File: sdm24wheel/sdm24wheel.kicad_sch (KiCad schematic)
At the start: 47 parts, among them J1 ATM15-08PA, J2 SWD, J3 USB_B_Micro, SW1 BOOT, U1 STM32F072CBT6, U2 MLX90614, U3 MIC37100-3.3WS, U4 24LC01BT-E/LT, U5 SN65HVD230, U6 USBLC6-2SC6, Y1 8MHz

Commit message: owo
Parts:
- C12: footprint Capacitor_SMD:C_0603_1608Metric -> Capacitor_SMD:C_0402_1005Metric
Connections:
- net CAN+: now also J1.1 (Pin_1); no longer J1.8 (Pin_8)
- net CAN-: now also J1.8 (Pin_8); no longer J1.1 (Pin_1)
- net GND: now also J1.2 (Pin_2), J1.3 (Pin_3); no longer J1.5 (Pin_5), J1.7 (Pin_7)
- net HE_OUTPUT: now also J1.5 (Pin_5), U1.40 (PB4); no longer J1.4 (Pin_4), U1.20 (PB2)
- net USR_LED: now also U1.13 (PA3); no longer U1.25 (PB12)
- net VCC: now also J1.6 (Pin_6), J1.7 (Pin_7); no longer J1.2 (Pin_2), J1.3 (Pin_3)
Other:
- moved on the sheet: D4, R6

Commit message: updating repo
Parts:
- removed C10, C13, C7, C8, C9: 100nF, Capacitor_SMD:C_0402_1005Metric, symbol Device:C_Small
- removed C11, C6: 4.7uF, Capacitor_SMD:C_0805_2012Metric, symbol Device:C_Small
- removed C12: 10nF, Capacitor_SMD:C_0402_1005Metric, symbol Device:C_Small
- removed C14, C15: 1uF, Capacitor_SMD:C_0805_2012Metric, symbol Device:C_Small
- removed D4: GREEN, Library:Dialight_561-XX0X-XXX, symbol Device:LED_Small
- removed FB1: 120R, Inductor_SMD:L_0603_1608Metric, symbol Device:FerriteBead_Small
- removed R4, R5: 4.7k, Resistor_SMD:R_0805_2012Metric, symbol Device:R_Small
- removed R6: 220, Resistor_SMD:R_0805_2012Metric, symbol Device:R_Small
- removed R7: 10k, Resistor_SMD:R_0805_2012Metric, symbol Device:R_Small
- removed SW1: BOOT, Library:Gravitech_MINI-SPDT-SW, symbol Switch:SW_SPDT
- removed U1: STM32F072CBT6, Package_QFP:LQFP-48_7x7mm_P0.5mm, symbol MCU_ST_STM32F0:STM32F072C8Tx
- removed Y1: 8MHz, Crystal:Crystal_SMD_Abracon_ABM3C-4Pin_5.0x3.2mm, symbol Device:Crystal_GND24
- added U1: STM32F405RGTx, Package_QFP:LQFP-64_10x10mm_P0.5mm, symbol MCU_ST_STM32F4:STM32F405RGTx
- C3, C5: value 10pF -> 2.2uF; footprint Capacitor_SMD:C_0603_1608Metric -> (none)
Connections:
- net +3.3V: now also U1.1 (VBAT), U1.19 (VDD), U1.32 (VDD), U1.48 (VDD), U1.64 (VDD)
- net +3.3VA: now also U1.13 (VDDA)
- net GND: now also U1.12 (VSSA), U1.18 (VSS), U1.63 (VSS)
- net HSE_IN: now also U1.5 (PH0); no longer C3.1
- net HSE_OUT: now also U1.6 (PH1); no longer C5.1
- net SWCLK: now also U1.49 (PA14)
- net SWDIO: now also U1.46 (PA13)
- new net: C5.1, U1.31 (VCAP_1)
- new net: C3.1, U1.47 (VCAP_2)
- new net NRST: U1.7 (NRST)
- new net SWO: U1.55 (PB3)
- no-connect marks 29 -> 4
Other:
- note added: "ESR < 2"
- note removed: "EA3250QA10-8.000M Load Capacitance: 10pF"
- note removed: "STM32F072x8"
- note removed: "disable internal pull-up/down resistors per 6.2 in datasheet"

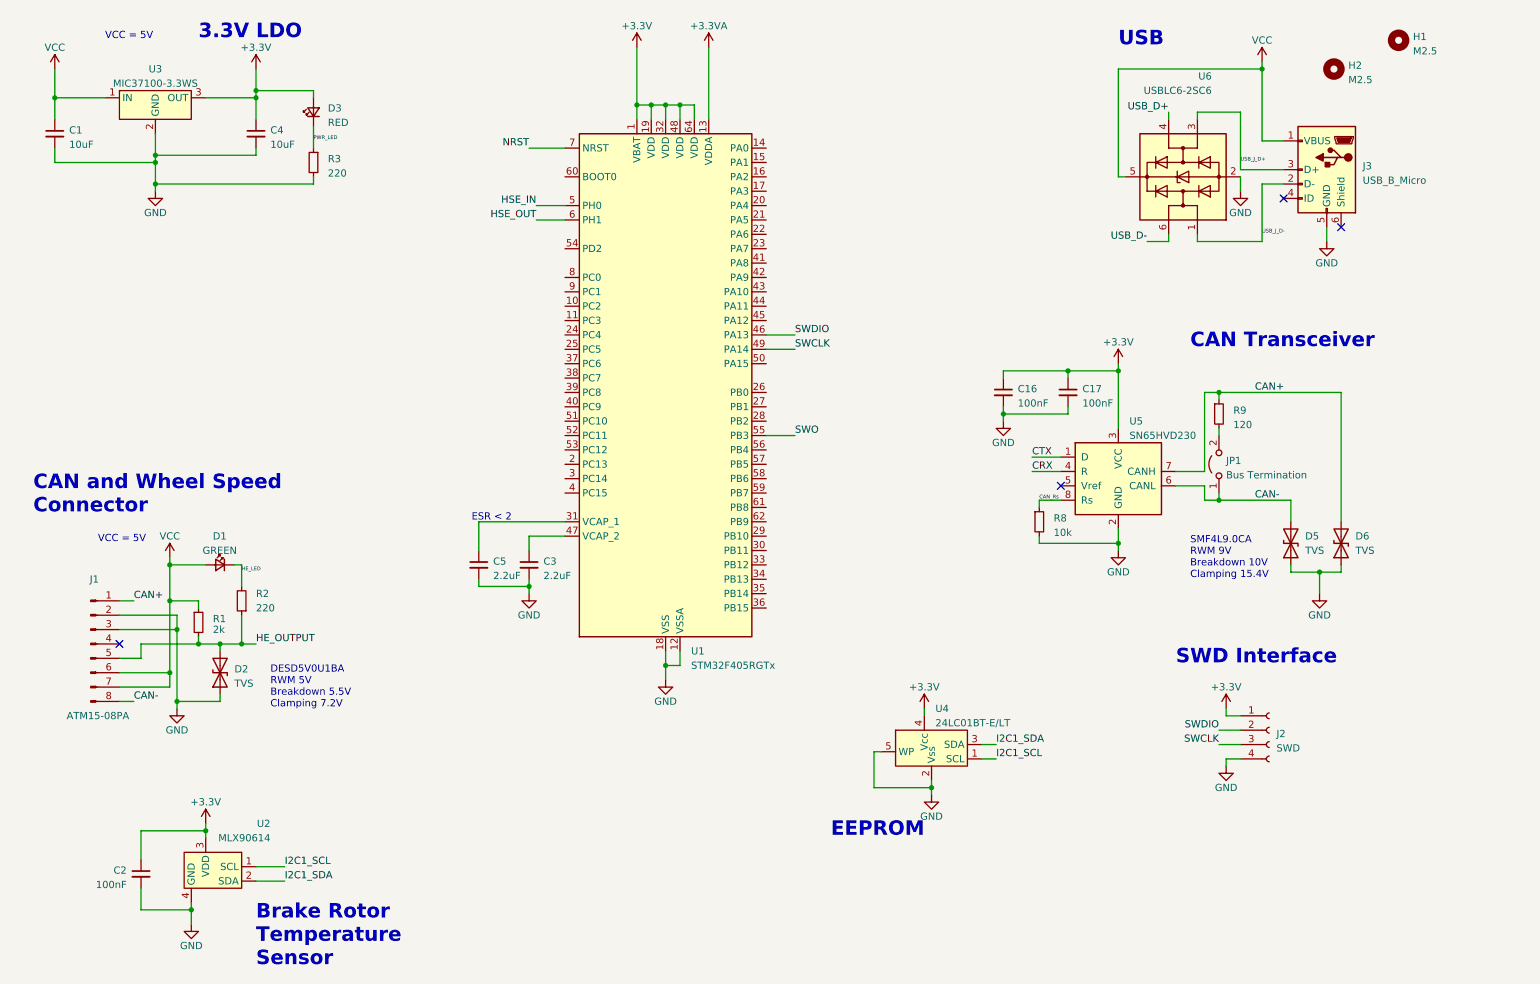
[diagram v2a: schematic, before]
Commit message: wheel board updates
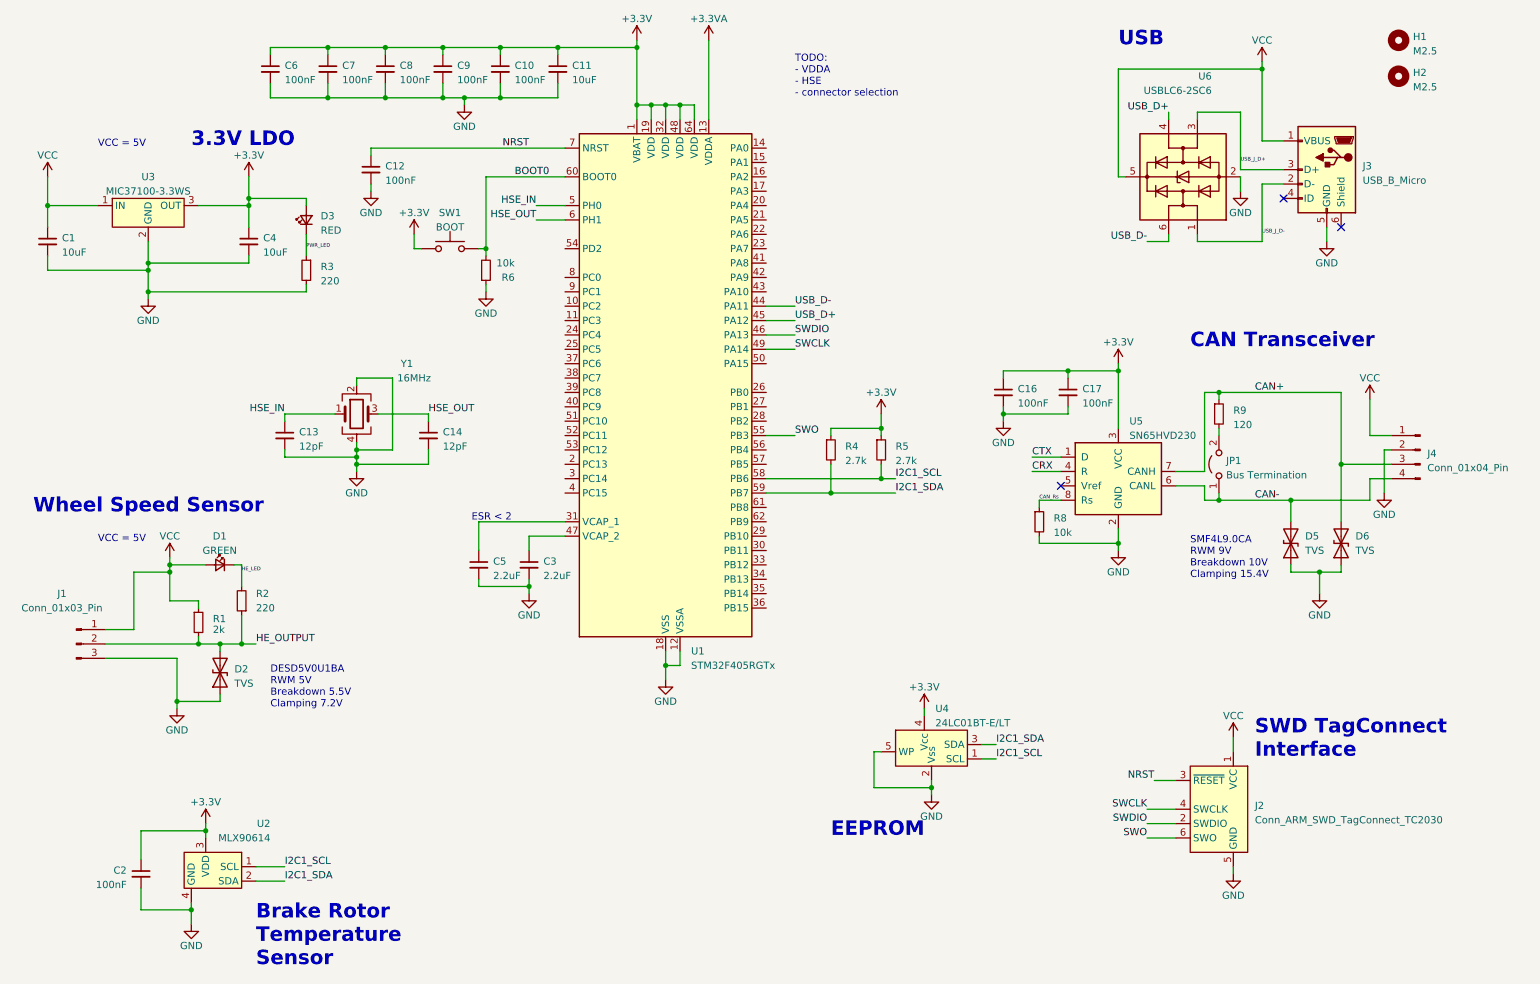
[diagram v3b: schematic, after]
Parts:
- removed J1: ATM15-08PA, Library:ATM15-08PX-BMXX, symbol Connector:Conn_01x08_Pin
- removed J2: SWD, Connector_PinSocket_2.54mm:PinSocket_1x04_P2.54mm_Vertical, symbol Connector:Conn_01x04_Socket
- added C10, C12, C6, C7, C8, C9: 100nF, symbol Device:C_Small
- added C11: 10uF, symbol Device:C_Small
- added C13, C14: 12pF, symbol Device:C_Small
- added J1: Conn_01x03_Pin, symbol Connector:Conn_01x03_Pin
- added J2: Conn_ARM_SWD_TagConnect_TC2030, Connector:Tag-Connect_TC2030-IDC-FP_2x03_P1.27mm_Vertical, symbol Connector:Conn_ARM_SWD_TagConnect_TC2030
- added J4: Conn_01x04_Pin, symbol Connector:Conn_01x04_Pin
- added R4, R5: 2.7k, Resistor_SMD:R_0805_2012Metric, symbol Device:R_Small
- added R6: 10k, Resistor_SMD:R_0805_2012Metric, symbol Device:R_Small
- added SW1: BOOT, symbol Switch:SW_Push
- added Y1: 16MHz, symbol Device:Crystal_GND24
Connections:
- net +3.3V: now also C10.1, C11.1, C6.1, C7.1, C8.1, C9.1, R4.1, R5.1, SW1.1
- net CAN+: now also J4.3 (Pin_3)
- net CAN-: now also J4.4 (Pin_4)
- net GND: now also C10.2, C11.2, C12.2, C13.2, C14.2, C6.2, C7.2, C8.2, C9.2, J1.3 (Pin_3), J2.5 (GND), J4.2 (Pin_2), R6.1, Y1.2, Y1.4
- net HE_OUTPUT: now also J1.2 (Pin_2)
- net HSE_IN: now also C13.1, Y1.1
- net HSE_OUT: now also C14.1, Y1.3
- net I2C1_SCL: now also U1.58 (PB6), R5.2
- net I2C1_SDA: now also U1.59 (PB7), R4.2
- net NRST: now also C12.1, J2.3 (~{RESET})
- net SWCLK: now also J2.4 (SWCLK)
- net SWDIO: now also J2.2 (SWDIO)
- net SWO: now also J2.6 (SWO)
- net USB_D+: now also U1.45 (PA12)
- net USB_D-: now also U1.44 (PA11)
- net VCC: now also J1.1 (Pin_1), J2.1 (VCC), J4.1 (Pin_1)
- net BOOT0: now reaches U1.60 (BOOT0)
- net BOOT0: now also R6.2, SW1.2
- no-connect marks 4 -> 3
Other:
- note added: "SWD TagConnect Interface"
- note added: "TODO: - VDDA - HSE - connector selection"
- note added: "Wheel Speed Sensor"
- note removed: "CAN and Wheel Speed Connector"
- note removed: "SWD Interface"
- moved on the sheet: C1, C4, D3, H2, R3, U3

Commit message: wheel board rework
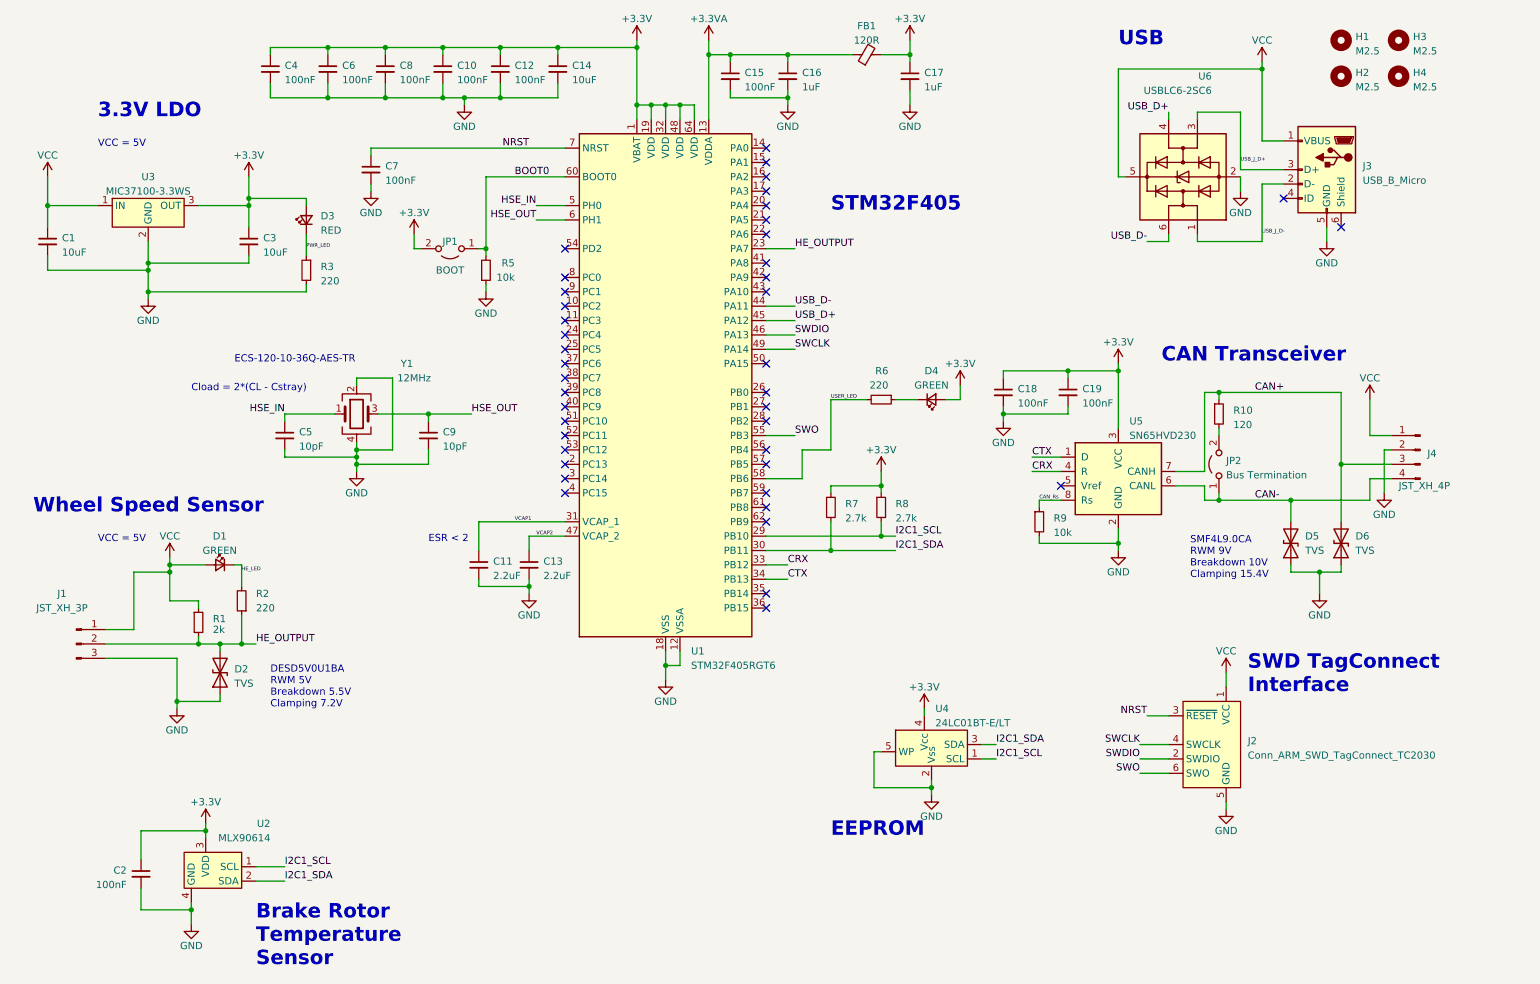
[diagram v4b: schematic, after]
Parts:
- removed R4, R5: 2.7k, Resistor_SMD:R_0805_2012Metric, symbol Device:R_Small
- removed SW1: BOOT, symbol Switch:SW_Push
- added C15: 100nF, Capacitor_SMD:C_0402_1005Metric, symbol Device:C_Small
- added C16, C17: 1uF, Capacitor_SMD:C_0603_1608Metric, symbol Device:C_Small
- added D4: GREEN, Library:Dialight_561-XX0X-XXX, symbol Device:LED_Small
- added FB1: 120R, Inductor_SMD:L_0603_1608Metric, symbol Device:FerriteBead_Small
- added H3, H4: M2.5, MountingHole:MountingHole_2.7mm_M2.5, symbol Mechanical:MountingHole
- added JP1: BOOT, Connector_PinHeader_2.54mm:PinHeader_1x02_P2.54mm_Vertical, symbol Jumper:Jumper_2_Open
- added R6: 220, Resistor_SMD:R_0805_2012Metric, symbol Device:R_Small
- added R7, R8: 2.7k, Resistor_SMD:R_0603_1608Metric, symbol Device:R_Small
- C10: renamed from C9; footprint (none) -> Capacitor_SMD:C_0402_1005Metric
- C11: renamed from C5; footprint (none) -> Capacitor_SMD:C_0603_1608Metric
- C12: renamed from C10; footprint (none) -> Capacitor_SMD:C_0402_1005Metric
- C13: renamed from C3; footprint (none) -> Capacitor_SMD:C_0603_1608Metric
- C14: renamed from C11; footprint (none) -> Capacitor_SMD:C_0805_2012Metric
- C4: renamed from C6; footprint (none) -> Capacitor_SMD:C_0402_1005Metric
- C5: renamed from C13; value 12pF -> 10pF; footprint (none) -> Capacitor_SMD:C_0402_1005Metric
- C6: renamed from C7; footprint (none) -> Capacitor_SMD:C_0402_1005Metric
- C7: renamed from C12; footprint (none) -> Capacitor_SMD:C_0402_1005Metric
- C8: footprint (none) -> Capacitor_SMD:C_0402_1005Metric
- C9: renamed from C14; value 12pF -> 10pF; footprint (none) -> Capacitor_SMD:C_0402_1005Metric
- J1: value Conn_01x03_Pin -> JST_XH_3P; footprint (none) -> Connector_JST:JST_XH_B3B-XH-AM_1x03_P2.50mm_Vertical
- J2: footprint Connector:Tag-Connect_TC2030-IDC-FP_2x03_P1.27mm_Vertical -> Connector:Tag-Connect_TC2030-IDC-NL_2x03_P1.27mm_Vertical
- J4: value Conn_01x04_Pin -> JST_XH_4P; footprint (none) -> Connector_JST:JST_XH_B4B-XH-AM_1x04_P2.50mm_Vertical
- U1: value STM32F405RGTx -> STM32F405RGT6
- Y1: value 16MHz -> 12MHz; footprint (none) -> Crystal:Crystal_SMD_2520-4Pin_2.5x2.0mm
- renumbered C16 to C18, C17 to C19, C4 to C3, JP1 to JP2, R9 to R10, R6 to R5, R8 to R9
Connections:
- net +3.3V: now also C17.1, D4.2 (A), FB1.2, JP1.2 (B), R7.1, R8.1
- net +3.3VA: now also C15.1, C16.1, FB1.1
- net BOOT0: now also JP1.1 (A)
- net CRX: now also U1.33 (PB12)
- net CTX: now also U1.34 (PB13)
- net GND: now also C15.2, C16.2, C17.2
- net HE_OUTPUT: now also U1.23 (PA7)
- net I2C1_SCL: now also U1.29 (PB10), R8.2; no longer U1.58 (PB6)
- net I2C1_SDA: now also U1.30 (PB11), R7.2; no longer U1.59 (PB7)
- net VCAP1: now reaches C11.1, U1.31 (VCAP_1)
- net VCAP2: now reaches C13.1, U1.47 (VCAP_2)
- new net: D4.1 (K), R6.1
- new net USER_LED: R6.2, U1.58 (PB6)
- no-connect marks 3 -> 41
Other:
- note added: "Cload = 2*(CL - Cstray)"
- note added: "ECS-120-10-36Q-AES-TR"
- note added: "STM32F405"
- note removed: "TODO: - VDDA - HSE - connector selection"
- moved on the sheet: H1, H2, J2

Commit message: adding updates
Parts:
- removed H1, H3: M2.5, MountingHole:MountingHole_2.7mm_M2.5, symbol Mechanical:MountingHole
- renumbered H2 to H1, H4 to H2
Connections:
- net HE_OUTPUT: now also U1.16 (PA2); no longer U1.23 (PA7)
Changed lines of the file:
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@@
   (title_block
     (title "SDM-24 Wheel Board")
-    (date "2023-09-03")
+    (date "2023-09-04")
     (rev "v1")
     (company "Sun Devil Motorsports")
@@
   (no_connect (at 144.78 46.99))
   (no_connect (at 144.78 118.11))
-  (no_connect (at 144.78 41.91))
   (no_connect (at 144.78 82.55))
   (no_connect (at 109.22 69.85))
   (no_connect (at 109.22 85.09))
   (no_connect (at 144.78 92.71))
+  (no_connect (at 144.78 54.61))
   (no_connect (at 109.22 77.47))
   (no_connect (at 144.78 52.07))
@@
     (stroke (width 0) (type default))
   )
+  (wire (pts (xy 144.78 41.91) (xy 149.86 41.91))
+    (stroke (width 0) (type default))
+  )
   (wire (pts (xy 222.25 99.06) (xy 222.25 96.52))
     (stroke (width 0) (type default))
@@
   )
   (wire (pts (xy 85.09 92.71) (xy 72.39 92.71))
-    (stroke (width 0) (type default))
-  )
-  (wire (pts (xy 144.78 54.61) (xy 149.86 54.61))
     (stroke (width 0) (type default))
   )
@@
     (effects (font (size 1.27 1.27)) (justify left bottom))
   )
-  (text "STM32F405" (at 156.21 48.26 0)
+  (text "STM32F405" (at 163.83 48.26 0)
     (effects (font (size 2.56 2.56) (thickness 0.512) bold) (justify left bottom))
   )
@@
     (effects (font (size 0.65 0.65)) (justify left bottom))
   )
-  (label "HE_OUTPUT" (at 149.86 54.61 0) (fields_autoplaced)
+  (label "HE_OUTPUT" (at 149.86 41.91 0) (fields_autoplaced)
     (effects (font (size 1.27 1.27)) (justify left bottom))
   )
@@
     )
   )
-  (symbol (lib_id "Mechanical:MountingHole") (at 256.54 17.78 0) (unit 1)
-    (in_bom yes) (on_board yes) (dnp no) (fields_autoplaced)
-    (property "Reference" "H3" (at 259.08 17.145 0)
-      (effects (font (size 1.27 1.27)) (justify left))
-    )
-    (property "Value" "M2.5" (at 259.08 19.685 0)
-      (effects (font (size 1.27 1.27)) (justify left))
-    )
-    (property "Footprint" "MountingHole:MountingHole_2.7mm_M2.5" (at 256.54 17.78 0)
-      (effects (font (size 1.27 1.27)) hide)
-    )
-    (property "Datasheet" "~" (at 256.54 17.78 0)
-      (effects (font (size 1.27 1.27)) hide)
-    )
-    (instances
-      (project "sdm24wheel"
-        (path "/58bd889d-28e2-49da-85df-8e04b7f08117"
-          (reference "H3") (unit 1)
-        )
-      )
-    )
-  )
   (symbol (lib_id "power:VCC") (at 17.78 41.91 0) (unit 1)
     (in_bom yes) (on_board yes) (dnp no) (fields_autoplaced)
@@
   (symbol (lib_id "Mechanical:MountingHole") (at 246.38 24.13 0) (unit 1)
     (in_bom yes) (on_board yes) (dnp no) (fields_autoplaced)
-    (property "Reference" "H2" (at 248.92 23.495 0)
+    (property "Reference" "H1" (at 248.92 23.495 0)
       (effects (font (size 1.27 1.27)) (justify left))
     )
@@
       (project "sdm24wheel"
         (path "/58bd889d-28e2-49da-85df-8e04b7f08117"
-          (reference "H2") (unit 1)
+          (reference "H1") (unit 1)
         )
       )
@@
   (symbol (lib_id "Mechanical:MountingHole") (at 256.54 24.13 0) (unit 1)
     (in_bom yes) (on_board yes) (dnp no) (fields_autoplaced)
-    (property "Reference" "H4" (at 259.08 23.495 0)
+    (property "Reference" "H2" (at 259.08 23.495 0)
       (effects (font (size 1.27 1.27)) (justify left))
     )
@@
       (project "sdm24wheel"
         (path "/58bd889d-28e2-49da-85df-8e04b7f08117"
-          (reference "H4") (unit 1)
-        )
-      )
-    )
-  )
-  (symbol (lib_id "Mechanical:MountingHole") (at 246.38 17.78 0) (unit 1)
-    (in_bom yes) (on_board yes) (dnp no) (fields_autoplaced)
-    (property "Reference" "H1" (at 248.92 17.145 0)
-      (effects (font (size 1.27 1.27)) (justify left))
-    )
-    (property "Value" "M2.5" (at 248.92 19.685 0)
-      (effects (font (size 1.27 1.27)) (justify left))
-    )
-    (property "Footprint" "MountingHole:MountingHole_2.7mm_M2.5" (at 246.38 17.78 0)
-      (effects (font (size 1.27 1.27)) hide)
-    )
-    (property "Datasheet" "~" (at 246.38 17.78 0)
-      (effects (font (size 1.27 1.27)) hide)
-    )
-    (instances
-      (project "sdm24wheel"
-        (path "/58bd889d-28e2-49da-85df-8e04b7f08117"
-          (reference "H1") (unit 1)
-        )
-      )
+          (reference "H2") (unit 1)
+        )
+      )
